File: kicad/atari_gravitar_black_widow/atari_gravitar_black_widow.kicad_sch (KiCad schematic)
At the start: 0 parts

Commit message: REVIEW
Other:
- note added: "DRG IN PROGRESS"
- note added: "JBB DONE IN Review"

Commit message: push
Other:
- note added: "DRG Done Needs FINAL"
- note removed: "DRG IN PROGRESS"

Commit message: reviewed first two sheets
see notes on individual sheets
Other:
- note added: "needs changes reviewed"

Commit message: Fri Night
various reviews
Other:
- note added: "bug check"
- note removed: "needs changes reviewed"

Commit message: REVIEWS AND FINALS
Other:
- note added: "DRG NEEDS BUG CHECK"
- note added: "JBB DONE NEEDS FINAL"
- note added: "JBB NEEDS FINAL"
- note added: "NEEDS BUG CHECK"
- note removed: "DRG Done Needs FINAL"
- note removed: "JBB DONE IN Review"
- note removed: "bug check"

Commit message: 20 errors left
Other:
- note removed: "JBB DONE Needs Review"

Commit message: Fixed most errors
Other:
- removed sheet Sheet8B
- added sheet Sheet 8B (untitled.kicad_sch)

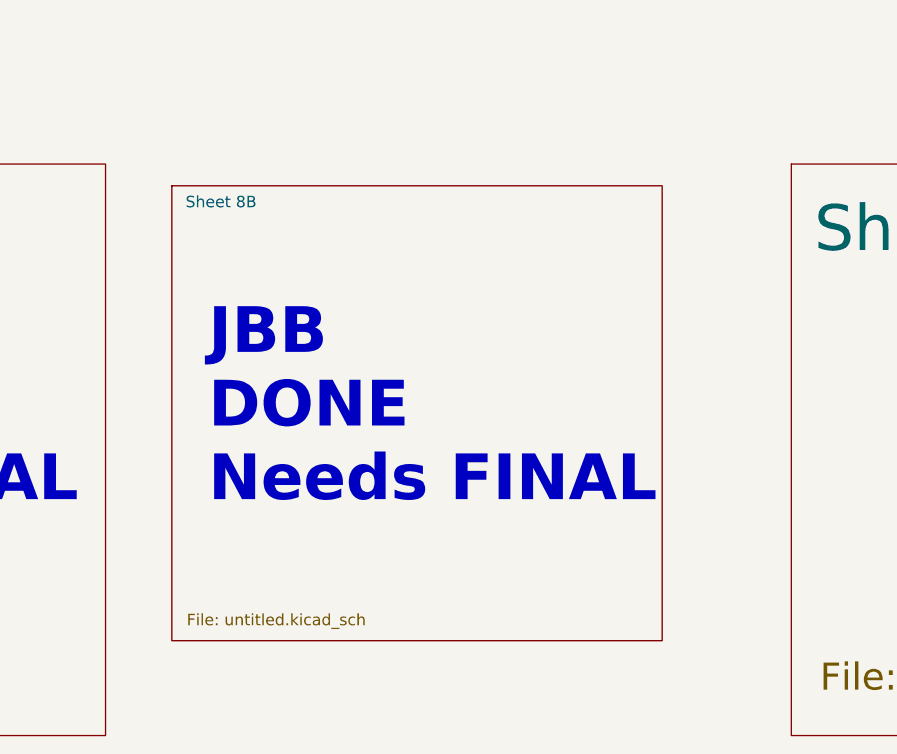
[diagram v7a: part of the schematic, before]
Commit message: Worked on removing the warnings
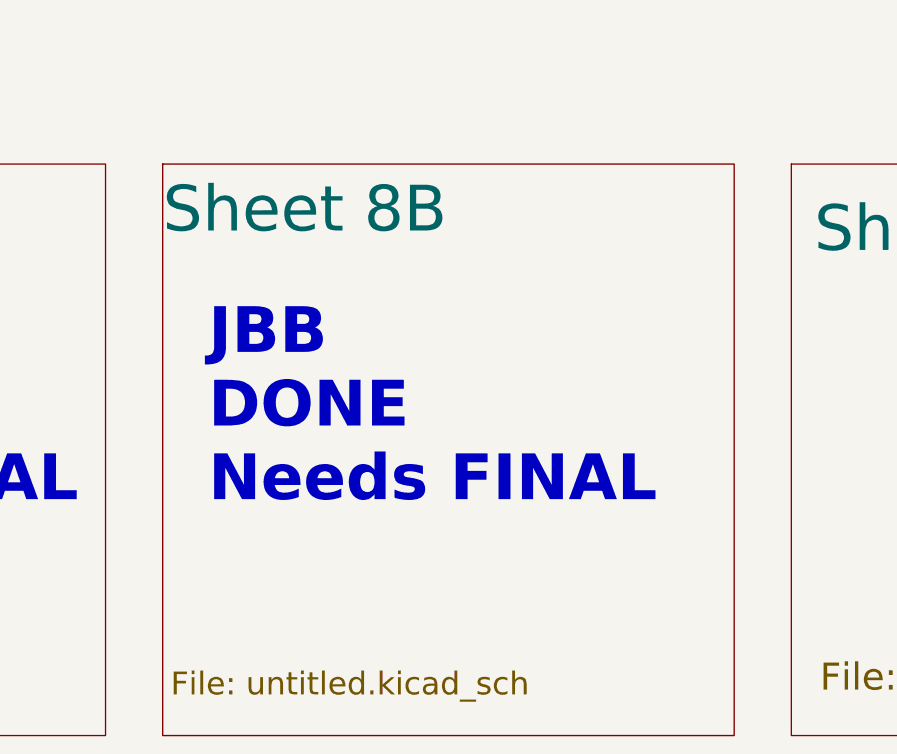
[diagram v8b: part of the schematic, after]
